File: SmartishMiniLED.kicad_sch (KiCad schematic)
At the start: 37 parts, among them J1 USB_C_Receptacle_USB2.0, J2 BUTTON, J3 Screw_Terminal_01x03, J4 Conn_01x02, P1 NeopixelStripPads, P2 NeopixelStripPads, Q1 MMBT2222, Q2 MMBT2222, Q3 IRLML6344, Q4 IRF7410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

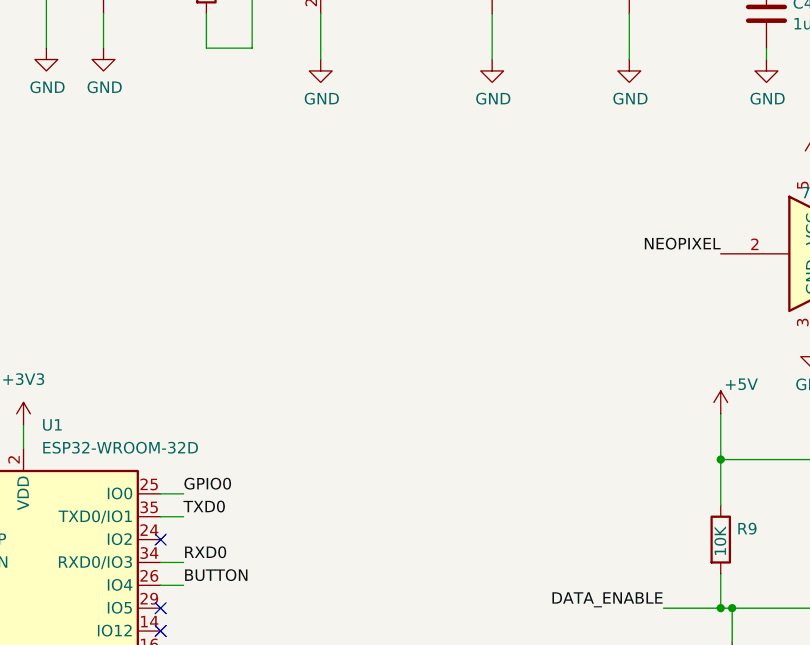
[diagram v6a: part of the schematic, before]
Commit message: Adding some power LEDs to help diagnose power issues.
Also various fixes to checks.
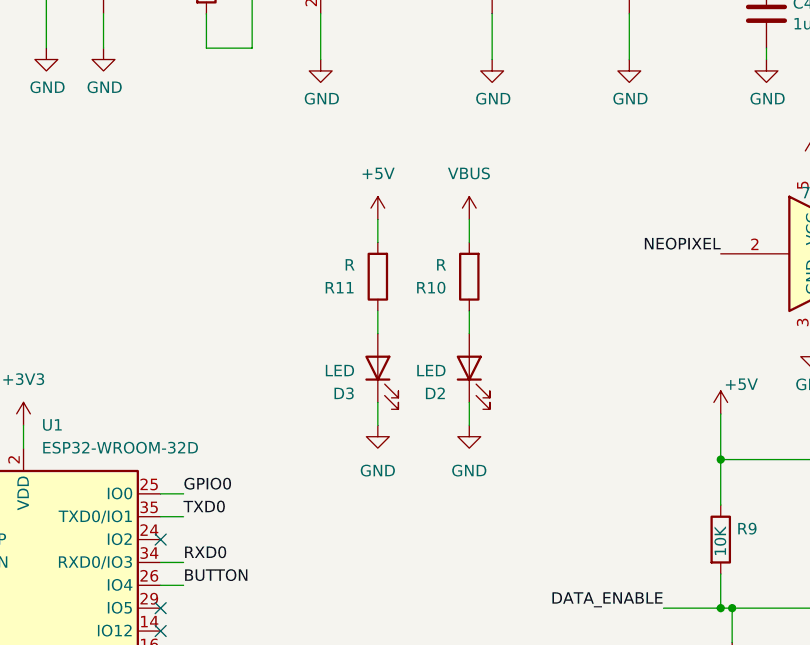
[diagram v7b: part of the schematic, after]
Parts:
- added D2, D3: LED, LED_SMD:LED_0805_2012Metric, symbol Device:LED
- added R10, R11: R, Resistor_SMD:R_0805_2012Metric, symbol Device:R
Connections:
- net +5V: now also R11.2
- net GND: now also D2.1 (K), D3.1 (K)
- net VBUS: now also R10.2
- new net: D2.2 (A), R10.1
- new net: D3.2 (A), R11.1
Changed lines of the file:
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@@
+    (stroke (width 0) (type default))
+  )
+  (wire (pts (xy 96.52 87.63) (xy 96.52 90.17))
     (stroke (width 0) (type default))
   )
@@
     (stroke (width 0) (type default))
   )
+  (wire (pts (xy 86.36 67.31) (xy 86.36 69.85))
+    (stroke (width 0) (type default))
+  )
   (wire (pts (xy 229.87 58.42) (xy 229.87 60.96))
     (stroke (width 0) (type default))
@@
     (stroke (width 0) (type default))
   )
+  (wire (pts (xy 86.36 87.63) (xy 86.36 90.17))
+    (stroke (width 0) (type default))
+  )
   (wire (pts (xy 198.12 115.57) (xy 203.2 115.57))
     (stroke (width 0) (type default))
@@
     (stroke (width 0) (type default))
   )
+  (wire (pts (xy 96.52 67.31) (xy 96.52 69.85))
+    (stroke (width 0) (type default))
+  )
   (wire (pts (xy 229.87 68.58) (xy 229.87 66.04))
     (stroke (width 0) (type default))
@@
     (stroke (width 0) (type default))
   )
+  (wire (pts (xy 96.52 77.47) (xy 96.52 80.01))
+    (stroke (width 0) (type default))
+  )
   (wire (pts (xy 113.03 129.54) (xy 113.03 132.08))
     (stroke (width 0) (type default))
@@
   )
   (wire (pts (xy 179.07 86.36) (xy 184.15 86.36))
+    (stroke (width 0) (type default))
+  )
+  (wire (pts (xy 86.36 77.47) (xy 86.36 80.01))
     (stroke (width 0) (type default))
   )
@@
     )
   )
+  (symbol (lib_id "Device:R") (at 96.52 73.66 180) (unit 1)
+    (in_bom yes) (on_board yes) (dnp no) (fields_autoplaced)
+    (property "Reference" "R10" (at 93.98 74.93 0)
+      (effects (font (size 1.27 1.27)) (justify left))
+    )
+    (property "Value" "R" (at 93.98 72.39 0)
+      (effects (font (size 1.27 1.27)) (justify left))
+    )
+    (property "Footprint" "Resistor_SMD:R_0805_2012Metric" (at 98.298 73.66 90)
+      (effects (font (size 1.27 1.27)) hide)
+    )
+    (property "Datasheet" "~" (at 96.52 73.66 0)
+      (effects (font (size 1.27 1.27)) hide)
+    )
+    (pin "1")
+    (pin "2")
+    (instances
+      (project "SmartishMiniLED"
+        (path "/3d6b945b-9848-4c53-9410-079f726f2f9f"
+          (reference "R10") (unit 1)
+        )
+      )
+    )
+  )
   (symbol (lib_id "power:VBUS") (at 30.48 27.94 0) (unit 1)
     (in_bom yes) (on_board yes) (dnp no)
@@
     )
   )
+  (symbol (lib_id "power:GND") (at 86.36 90.17 0) (unit 1)
+    (in_bom yes) (on_board yes) (dnp no) (fields_autoplaced)
+    (property "Reference" "#PWR021" (at 86.36 96.52 0)
+      (effects (font (size 1.27 1.27)) hide)
+    )
+    (property "Value" "GND" (at 86.36 95.25 0)
+      (effects (font (size 1.27 1.27)))
+    )
+    (property "Footprint" "" (at 86.36 90.17 0)
+      (effects (font (size 1.27 1.27)) hide)
+    )
+    (property "Datasheet" "" (at 86.36 90.17 0)
+      (effects (font (size 1.27 1.27)) hide)
+    )
+    (pin "1")
+    (instances
+      (project "SmartishMiniLED"
+        (path "/3d6b945b-9848-4c53-9410-079f726f2f9f"
+          (reference "#PWR021") (unit 1)
+        )
+      )
+    )
+  )
   (symbol (lib_id "power:GND") (at 217.17 43.18 0) (unit 1)
     (in_bom yes) (on_board yes) (dnp no)
@@
         (path "/3d6b945b-9848-4c53-9410-079f726f2f9f"
           (reference "#PWR011") (unit 1)
+        )
+      )
+    )
+  )
+  (symbol (lib_id "power:GND") (at 96.52 90.17 0) (unit 1)
+    (in_bom yes) (on_board yes) (dnp no) (fields_autoplaced)
+    (property "Reference" "#PWR022" (at 96.52 96.52 0)
+      (effects (font (size 1.27 1.27)) hide)
+    )
+    (property "Value" "GND" (at 96.52 95.25 0)
+      (effects (font (size 1.27 1.27)))
+    )
+    (property "Footprint" "" (at 96.52 90.17 0)
+      (effects (font (size 1.27 1.27)) hide)
+    )
+    (property "Datasheet" "" (at 96.52 90.17 0)
+      (effects (font (size 1.27 1.27)) hide)
+    )
+    (pin "1")
+    (instances
+      (project "SmartishMiniLED"
+        (path "/3d6b945b-9848-4c53-9410-079f726f2f9f"
+          (reference "#PWR022") (unit 1)
         )
       )
@@
     )
   )
+  (symbol (lib_id "Device:LED") (at 96.52 83.82 90) (unit 1)
+    (in_bom yes) (on_board yes) (dnp no) (fields_autoplaced)
+    (property "Reference" "D2" (at 93.98 86.6775 90)
+      (effects (font (size 1.27 1.27)) (justify left))
+    )
+    (property "Value" "LED" (at 93.98 84.1375 90)
+      (effects (font (size 1.27 1.27)) (justify left))
+    )
+    (property "Footprint" "LED_SMD:LED_0805_2012Metric" (at 96.52 83.82 0)
+      (effects (font (size 1.27 1.27)) hide)
+    )
+    (property "Datasheet" "~" (at 96.52 83.82 0)
+      (effects (font (size 1.27 1.27)) hide)
+    )
+    (pin "2")
+    (pin "1")
+    (instances
+      (project "SmartishMiniLED"
+        (path "/3d6b945b-9848-4c53-9410-079f726f2f9f"
+          (reference "D2") (unit 1)
+        )
+      )
+    )
+  )
   (symbol (lib_id "power:GND") (at 181.61 81.28 180) (unit 1)
     (in_bom yes) (on_board yes) (dnp no)
@@
     )
   )
+  (symbol (lib_id "power:VBUS") (at 96.52 67.31 0) (unit 1)
+    (in_bom yes) (on_board yes) (dnp no) (fields_autoplaced)
+    (property "Reference" "#PWR024" (at 96.52 71.12 0)
+      (effects (font (size 1.27 1.27)) hide)
+    )
+    (property "Value" "VBUS" (at 96.52 62.23 0)
+      (effects (font (size 1.27 1.27)))
+    )
+    (property "Footprint" "" (at 96.52 67.31 0)
+      (effects (font (size 1.27 1.27)) hide)
+    )
+    (property "Datasheet" "" (at 96.52 67.31 0)
+      (effects (font (size 1.27 1.27)) hide)
+    )
+    (pin "1")
+    (instances
+      (project "SmartishMiniLED"
+        (path "/3d6b945b-9848-4c53-9410-079f726f2f9f"
+          (reference "#PWR024") (unit 1)
+        )
+      )
+    )
+  )
   (symbol (lib_id "power:+5V") (at 20.32 26.67 0) (unit 1)
     (in_bom yes) (on_board yes) (dnp no)
@@
         (path "/3d6b945b-9848-4c53-9410-079f726f2f9f"
           (reference "#PWR017") (unit 1)
+        )
+      )
+    )
+  )
+  (symbol (lib_id "Device:R") (at 86.36 73.66 180) (unit 1)
+    (in_bom yes) (on_board yes) (dnp no) (fields_autoplaced)
+    (property "Reference" "R11" (at 83.82 74.93 0)
+      (effects (font (size 1.27 1.27)) (justify left))
+    )
+    (property "Value" "R" (at 83.82 72.39 0)
+      (effects (font (size 1.27 1.27)) (justify left))
+    )
+    (property "Footprint" "Resistor_SMD:R_0805_2012Metric" (at 88.138 73.66 90)
+      (effects (font (size 1.27 1.27)) hide)
+    )
+    (property "Datasheet" "~" (at 86.36 73.66 0)
+      (effects (font (size 1.27 1.27)) hide)
+    )
+    (pin "1")
+    (pin "2")
+    (instances
+      (project "SmartishMiniLED"
+        (path "/3d6b945b-9848-4c53-9410-079f726f2f9f"
+          (reference "R11") (unit 1)
         )
       )
@@
         (path "/3d6b945b-9848-4c53-9410-079f726f2f9f"
           (reference "#PWR06") (unit 1)
+        )
+      )
+    )
+  )
+  (symbol (lib_id "Device:LED") (at 86.36 83.82 90) (unit 1)
+    (in_bom yes) (on_board yes) (dnp no) (fields_autoplaced)
+    (property "Reference" "D3" (at 83.82 86.6775 90)
+      (effects (font (size 1.27 1.27)) (justify left))
+    )
+    (property "Value" "LED" (at 83.82 84.1375 90)
+      (effects (font (size 1.27 1.27)) (justify left))
+    )
+    (property "Footprint" "LED_SMD:LED_0805_2012Metric" (at 86.36 83.82 0)
+      (effects (font (size 1.27 1.27)) hide)
+    )
+    (property "Datasheet" "~" (at 86.36 83.82 0)
+      (effects (font (size 1.27 1.27)) hide)
+    )
+    (pin "1")
+    (pin "2")
+    (instances
+      (project "SmartishMiniLED"
+        (path "/3d6b945b-9848-4c53-9410-079f726f2f9f"
+          (reference "D3") (unit 1)
         )
       )
@@
         )
       )
+    )
+  )
+  (symbol (lib_id "power:+5V") (at 86.36 67.31 0) (unit 1)
+    (in_bom yes) (on_board yes) (dnp no) (fields_autoplaced)
+    (property "Reference" "#PWR023" (at 86.36 71.12 0)
+      (effects (font (size 1.27 1.27)) hide)
+    )
+    (property "Value" "+5V" (at 86.36 62.23 0)
+      (effects (font (size 1.27 1.27)))
+    )
+    (property "Footprint" "" (at 86.36 67.31 0)
+      (effects (font (size 1.27 1.27)) hide)
+    )
+    (property "Datasheet" "" (at 86.36 67.31 0)
+      (effects (font (size 1.27 1.27)) hide)
+    )
+    (pin "1")
+    (instances
+      (project "SmartishMiniLED"
+        (path "/3d6b945b-9848-4c53-9410-079f726f2f9f"
+          (reference "#PWR023") (unit 1)
+        )
+      )
